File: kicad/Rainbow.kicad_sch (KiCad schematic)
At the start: 22 parts, among them J1 PICKit3, J2 UART, J3 JUMPER, J4 JACK, J5 RGB, J6 RGB, J7 RGB, J8 RGB, J9 SOURCE, Q1 2N7000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

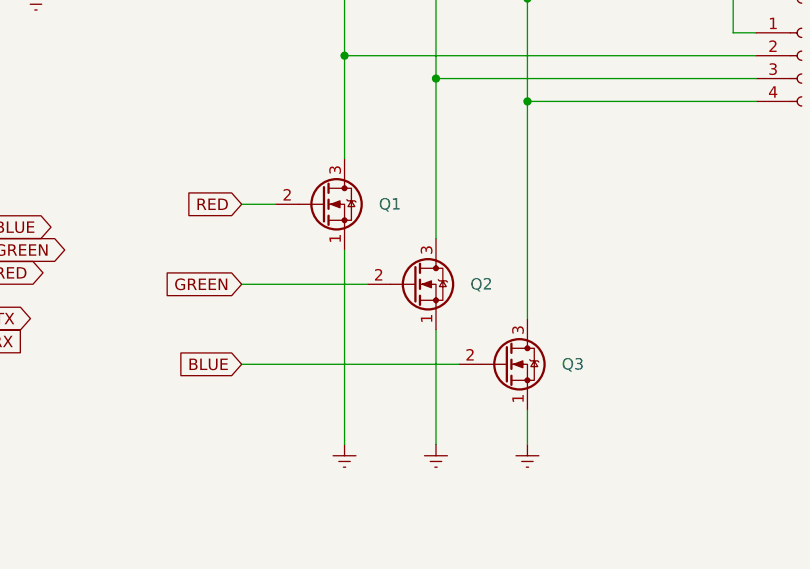
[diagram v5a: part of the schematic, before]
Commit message: Fix FET pins and traces
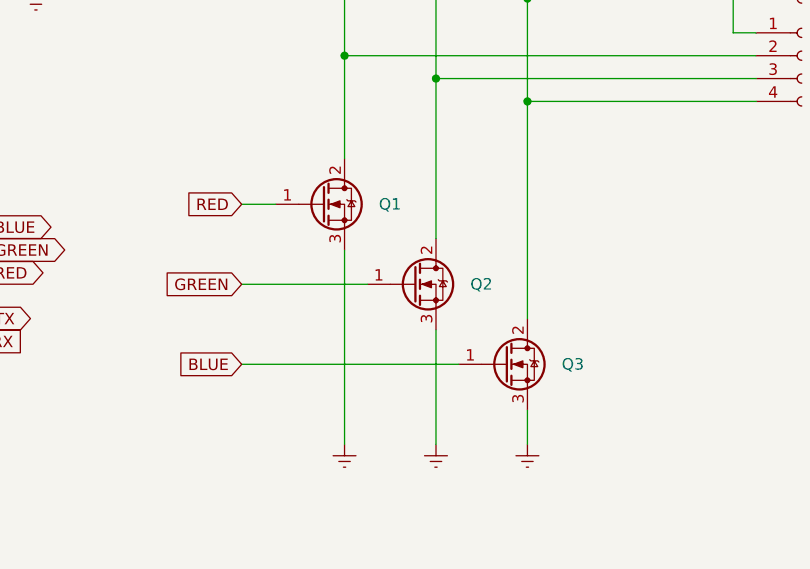
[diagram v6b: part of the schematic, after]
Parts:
- removed Q1, Q2, Q3: 2N7000, Package_TO_SOT_THT:TO-220-3_Vertical, symbol Transistor_FET:2N7000
- added Q1, Q2, Q3: Q_NMOS_GDS, Package_TO_SOT_THT:TO-220-3_Vertical, symbol Device:Q_NMOS_GDS
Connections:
- net BLUE: now also Q3.1 (G)
- net GNDREF: now also Q1.3 (S), Q2.3 (S), Q3.3 (S)
- net GREEN: now also Q2.1 (G)
- net RED: now also Q1.1 (G)
- net at J5.2 (Pin_2), J6.2 (Pin_2), J7.2 (Pin_2)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: now also Q1.2 (D)
- net at J5.3 (Pin_3), J6.3 (Pin_3), J7.3 (Pin_3)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: now also Q2.2 (D)
- net at J5.4 (Pin_4), J6.4 (Pin_4), J7.4 (Pin_4)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: now also Q3.2 (D)
